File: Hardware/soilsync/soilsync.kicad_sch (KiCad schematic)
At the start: 20 parts, among them J1 Barrel_Jack_Switch, J10 Screw_Terminal_01x03, J11 Screw_Terminal_01x03, J12 Screw_Terminal_01x03, J13 Screw_Terminal_01x02, J2 Screw_Terminal_01x03, J3 Screw_Terminal_01x03, J4 Screw_Terminal_01x03, J5 Screw_Terminal_01x03, J6 Screw_Terminal_01x03, J7 Screw_Terminal_01x03, J8 Screw_Terminal_01x03, J9 Screw_Terminal_01x03, U1 STM32F103C8Tx, U2 LM2596, U3 NRF24L01_Breakout, U4 AMS1117-3.3, U5 TP5100

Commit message: finishing PCB
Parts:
- removed J13: Screw_Terminal_01x02, symbol Connector:Screw_Terminal_01x02
- added J13: Conn_Battery, TerminalBlock_4Ucon:TerminalBlock_4Ucon_1x03_P3.50mm_Horizontal, symbol Connector:Screw_Terminal_01x03
- added U6: HX-2S, CustomModule:HX-2S BMS module, symbol CustomModule:HX-2S-JH20_V1.0
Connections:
- net BAT+: now also D2.2 (A), U6.3 (P+)
- net GND: now also U6.4 (P-)
- net NRF_MISO: no longer U1.28 (PB15)
- net NRF_MOSI: now also U1.28 (PB15)
- net VIN: now also U5.3 (VCC)
- new net: J13.1 (Pin_1), U6.2 (B-)
- new net: J13.2 (Pin_2), U6.5 (BM)
- new net: J13.3 (Pin_3), U6.1 (B+)
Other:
- moved on the sheet: D2

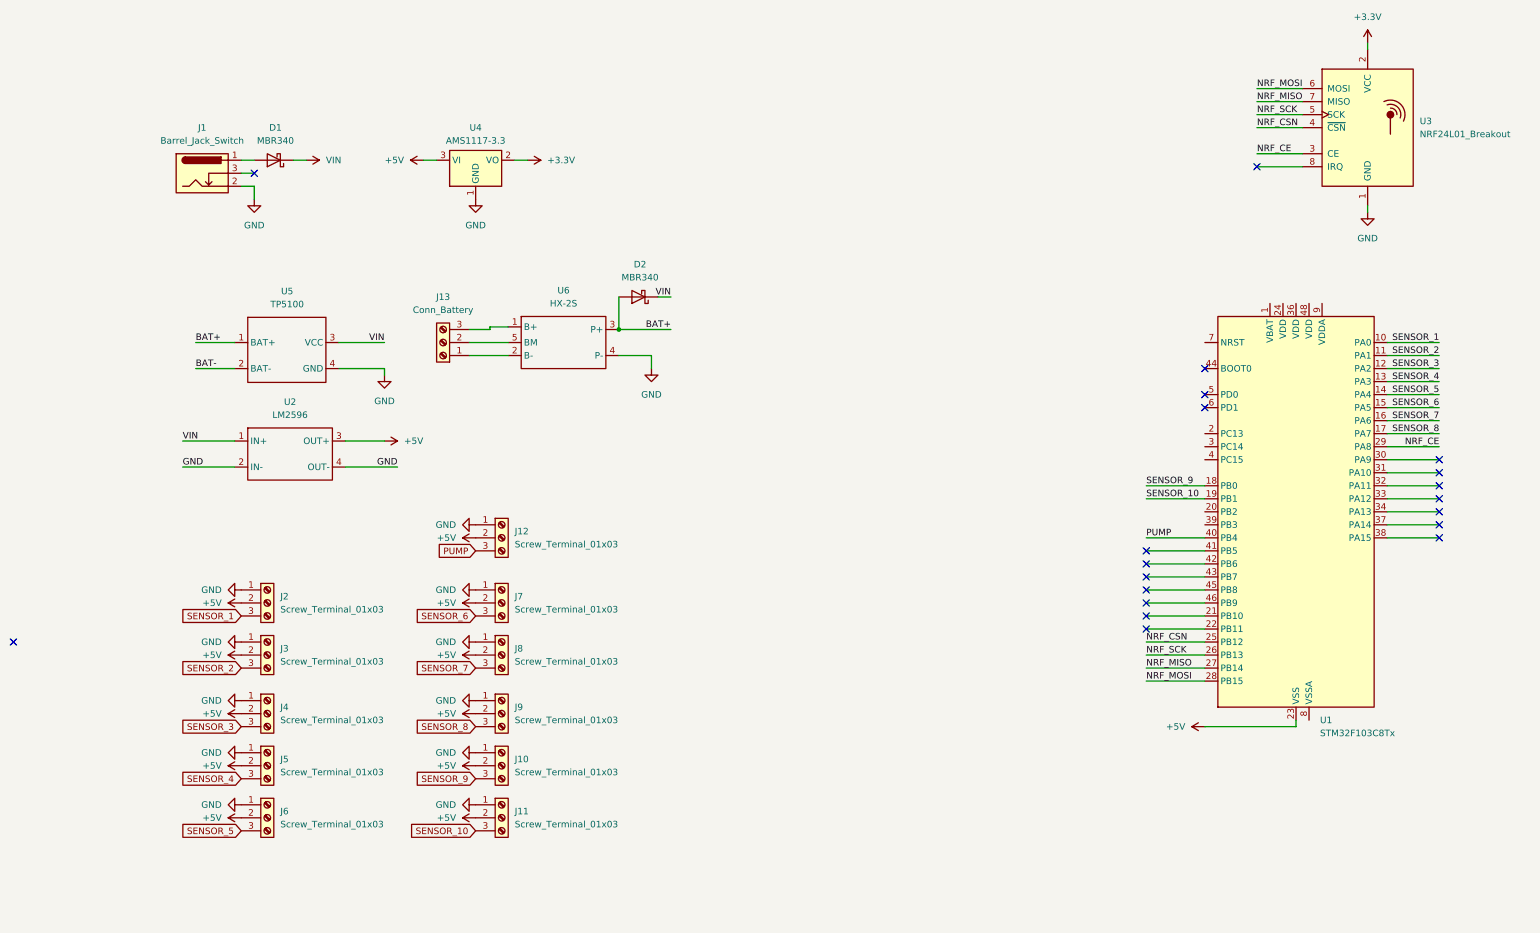
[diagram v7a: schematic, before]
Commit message: layout nearly finished.
need to add mosfet and programming connector
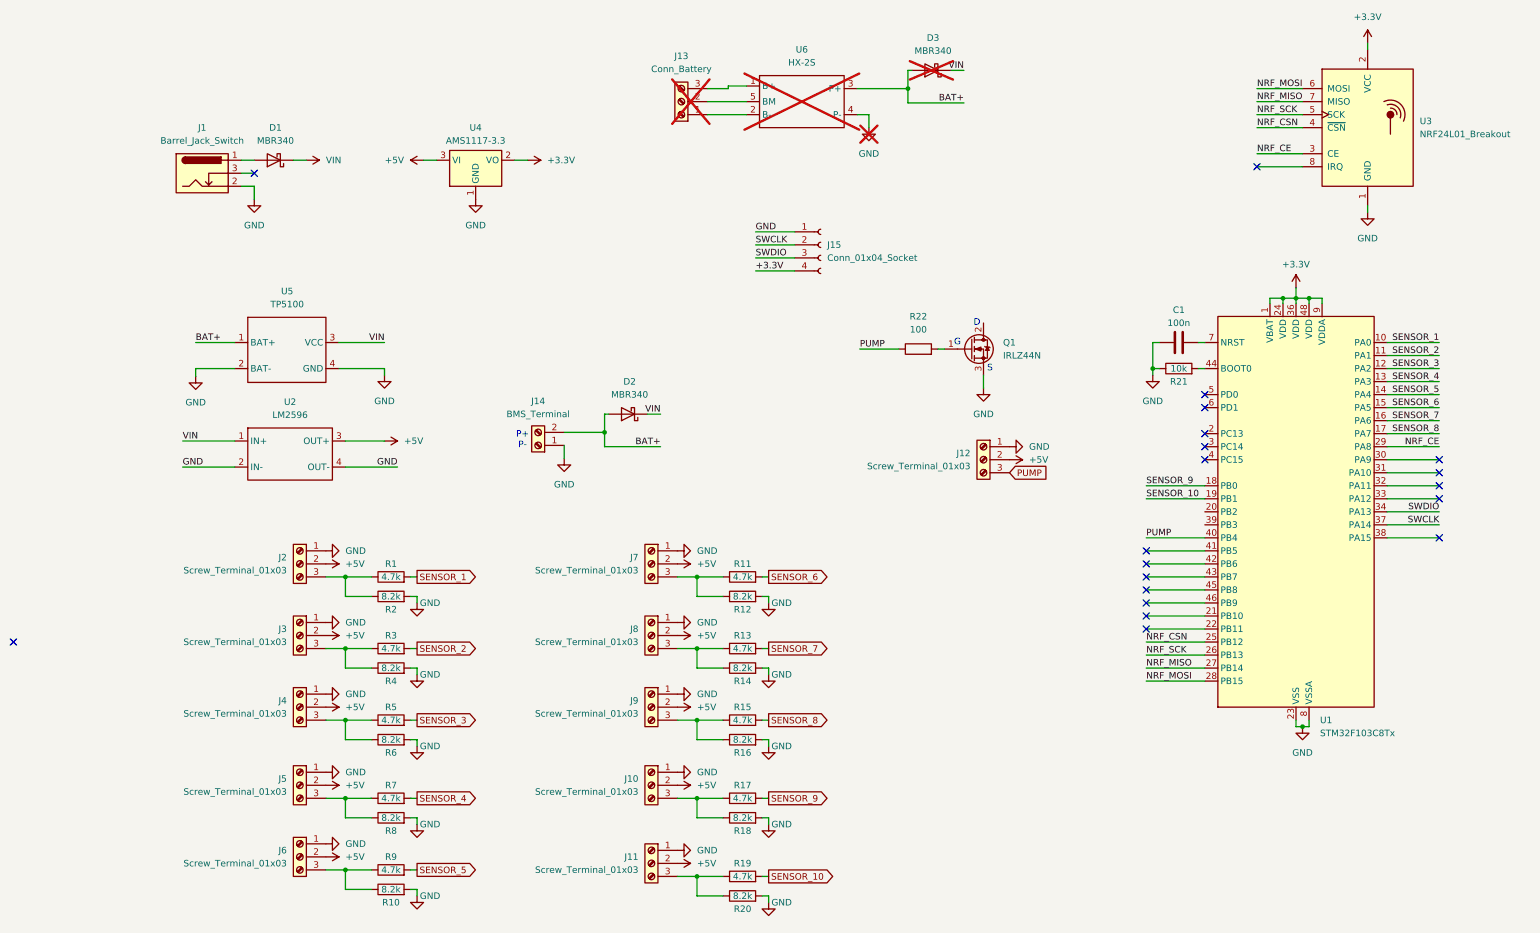
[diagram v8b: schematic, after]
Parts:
- added C1: 100n, Capacitor_SMD:C_1206_3216Metric_Pad1.33x1.80mm_HandSolder, symbol Device:C
- added D3: MBR340, Diode_THT:D_DO-201AD_P15.24mm_Horizontal, symbol Diode:MBR340
- added J14: BMS_Terminal, TerminalBlock_4Ucon:TerminalBlock_4Ucon_1x02_P3.50mm_Horizontal, symbol Connector:Screw_Terminal_01x02
- added J15: Conn_01x04_Socket, Connector_PinSocket_2.54mm:PinSocket_1x04_P2.54mm_Vertical, symbol Connector:Conn_01x04_Socket
- added Q1: IRLZ44N, Package_TO_SOT_THT:TO-220-3_Vertical, symbol Transistor_FET:IRLZ44N
- added R1, R11, R13, R15, R17, R19, R3, R5, R7, R9: 4.7k, Resistor_SMD:R_0805_2012Metric, symbol Device:R
- added R10, R12, R14, R16, R18, R2, R20, R4, R6, R8: 8.2k, Resistor_SMD:R_0805_2012Metric, symbol Device:R
- added R21: 10k, Resistor_SMD:R_1206_3216Metric_Pad1.30x1.75mm_HandSolder, symbol Device:R
- added R22: 100, symbol Device:R
- J13, U6: now not fitted
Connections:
- net BAT- is gone; now on net GND: U5.2 (BAT-)
- net +3.3V: now also U1.1 (VBAT), U1.24 (VDD), U1.36 (VDD), U1.48 (VDD), U1.9 (VDDA), J15.4 (Pin_4)
- net +5V: no longer U1.23 (VSS), U1.35 (VSS), U1.47 (VSS)
- net BAT+: now also D3.2 (A), J14.2 (Pin_2)
- net GND: now also U1.23 (VSS), U1.35 (VSS), U1.47 (VSS), U1.8 (VSSA), C1.1, J14.1 (Pin_1), J15.1 (Pin_1), Q1.3 (S), R10.2, R12.2, R14.2, R16.2, R18.2, R2.2, R20.2, R21.1, R4.2, R6.2, R8.2
- net PUMP: now also R22.1
- net SENSOR_1: now also R1.2; no longer J2.3 (Pin_3)
- net SENSOR_10: now also R19.2; no longer J11.3 (Pin_3)
- net SENSOR_2: now also R3.2; no longer J3.3 (Pin_3)
- net SENSOR_3: now also R5.2; no longer J4.3 (Pin_3)
- net SENSOR_4: now also R7.2; no longer J5.3 (Pin_3)
- net SENSOR_5: now also R9.2; no longer J6.3 (Pin_3)
- net SENSOR_6: now also R11.2; no longer J7.3 (Pin_3)
- net SENSOR_7: now also R13.2; no longer J8.3 (Pin_3)
- net SENSOR_8: now also R15.2; no longer J9.3 (Pin_3)
- net SENSOR_9: now also R17.2; no longer J10.3 (Pin_3)
- net VIN: now also D3.1 (K)
- net SWDIO: now reaches U1.34 (PA13)
- net SWDIO: now also J15.3 (Pin_3)
- net SWCLK: now reaches U1.37 (PA14)
- net SWCLK: now also J15.2 (Pin_2)
- net at U1.44 (BOOT0): now also R21.2
- net at U1.7 (NRST): now also C1.2
- new net: J7.3 (Pin_3), R11.1, R12.1
- new net: J2.3 (Pin_3), R1.1, R2.1
- new net: J11.3 (Pin_3), R19.1, R20.1
- new net: J5.3 (Pin_3), R7.1, R8.1
- new net: J4.3 (Pin_3), R5.1, R6.1
- new net: J3.3 (Pin_3), R3.1, R4.1
- new net: J10.3 (Pin_3), R17.1, R18.1
- new net: J9.3 (Pin_3), R15.1, R16.1
- new net: J8.3 (Pin_3), R13.1, R14.1
- new net: Q1.1 (G), R22.2
- new net: J6.3 (Pin_3), R10.1, R9.1
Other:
- note added: "D"
- note added: "G"
- note added: "P+ P-"
- note added: "S"
- moved on the sheet: D2, J10, J11, J12, J2, J3, J4, J5, J6, J7, J8, J9
